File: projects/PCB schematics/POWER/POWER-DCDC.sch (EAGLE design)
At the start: 1 part

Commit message: POWER - DC DC 90% done.
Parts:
- added C1: 1u, rcl:C-USC0805
- added C2, C3: ECA-1VM102B, IowaFormula:ECA-1VM102B
- added F1: 0505030.MXEP, IowaFormula:0505030.MXEP
- added J3, J4: 2P_1-770166-0, con-MATE-N-LOK:2P_1-770166-0
- added R1: PWR221T-30-1R00F, IowaFormula:PWR221T-30-1R00F
- added U$1: DCMHEATSINK, IowaFormula:DCMHEATSINK
- added U$2: SRP1238A-R22M, IowaFormula:SRP1238A-R22M
- added U$3: SRP1238A-4R7M, IowaFormula:SRP1238A-4R7M
- added X1, X2, X3, X4: 5566-2, con-molex:5566-2
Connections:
- new net +12V-ISO: X1-1.S, X1-2.S, X2-1.S, X2-2.S
- new net +12V-OUT: C1.1, C2.1, C3.1, PS1.+OUT_1, R1.1, U$2.1
- new net GND: C1.2, C2.2, C3.2, PS1.-OUT_1, X3-1.S, X3-2.S, X4-1.S, X4-2.S
- new net HV+: F1.1, J3.1, J3.2
- new net HV+_IN: PS1.+IN, U$3.2
- new net HV+_POSTFUSE: F1.2, U$3.1
- new net HV-: J4.1, J4.2, PS1.-IN
- new net N$1: R1.2, U$2.2
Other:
- note added: "30A 0505030.MXEP 500VAC/VDC"
- moved on the sheet: PS1

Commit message: POWER - DCDC Rev A.
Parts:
- removed U$2: SRP1238A-R22M, IowaFormula:SRP1238A-R22M
- removed X3, X4: 5566-2, con-molex:5566-2
- added .GND, >GND: 5566-2, con-molex:5566-2
- added C14, C4, C5, C7: ECA-2WHG2R2, IowaFormula:ECA-2WHG2R2
- added R2: PWR221T-30-1R00F, IowaFormula:PWR221T-30-1R00F
- added U$4: SRP1238A-4R7M, IowaFormula:SRP1238A-4R7M
- C1: value 1u -> ECA-2WHG2R2; device rcl:C-USC0805 -> IowaFormula:ECA-2WHG2R2
- renumbered J3 to HV+, J4 to HV-, X1 to +12V-ISO1, X2 to +12V-ISO2
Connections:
- removed net HV+_IN: PS1.+IN, U$3.2
- net +12V-ISO: now also C14.1, C5.1, R1.2, U$4.2
- net +12V-OUT: now also U$4.1; no longer C1.1, U$2.1
- net GND: now also .GND-1.S, .GND-2.S, >GND-1.S, >GND-2.S, C14.2, C5.2; no longer C1.2, X3-1.S, X3-2.S, X4-1.S, X4-2.S
- net HV+_POSTFUSE: now also R2.2
- net HV-: now also C1.2, C4.2, C7.2
- net N$1: now also C1.1, C4.1, C7.1, PS1.+IN, R2.1, U$3.2; no longer R1.2, U$2.2
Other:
- moved on the sheet: C2, C3, F1, R1, U$3

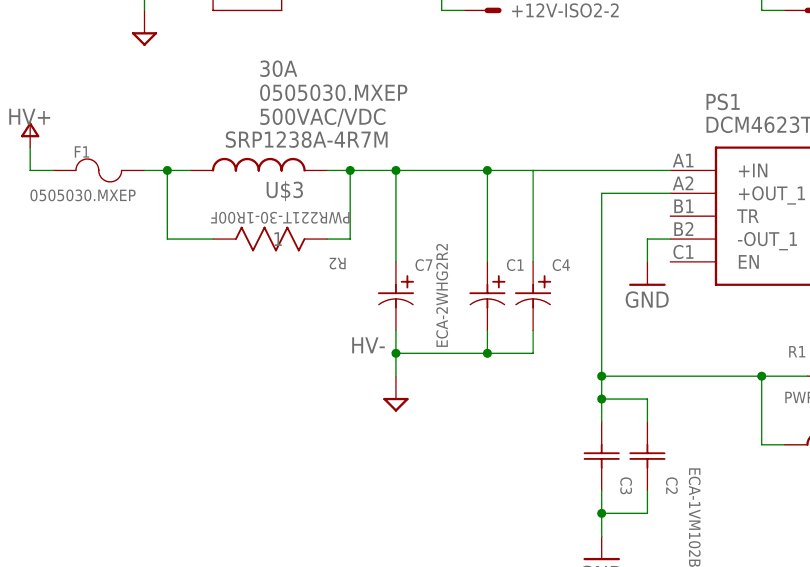
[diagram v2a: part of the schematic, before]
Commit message: POWER - DCDC changes w/ Ryan.
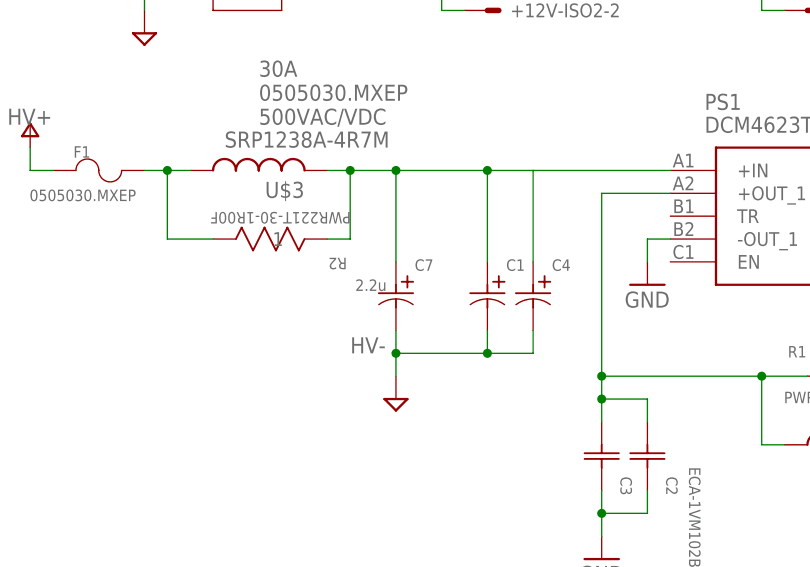
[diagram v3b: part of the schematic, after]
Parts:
- C7: value ECA-2WHG2R2 -> 2.2u
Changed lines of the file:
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@@
 <part name="R1" library="IowaFormula" deviceset="PWR221T-30-1R00F" device=""/>
 <part name="U$3" library="IowaFormula" deviceset="SRP1238A-4R7M" device=""/>
-<part name="C7" library="IowaFormula" deviceset="ECA-2WHG2R2" device=""/>
+<part name="C7" library="IowaFormula" deviceset="ECA-2WHG2R2" device="" value="2.2u"/>
 <part name="SUPPLY3" library="supply2" library_urn="urn:adsk.eagle:library:372" deviceset="AGND" device=""/>
 <part name="R2" library="IowaFormula" deviceset="PWR221T-30-1R00F" device=""/>
@@
 </instance>
 <instance part="C7" gate="A" x="40.64" y="35.56" smashed="yes" rot="R270">
-<attribute name="VALUE" x="46.4058" y="25.9588" size="1.27" layer="96" ratio="10" rot="SR90"/>
+<attribute name="VALUE" x="36.1188" y="32.3342" size="1.27" layer="96" ratio="10" rot="SR0"/>
 <attribute name="NAME" x="42.7228" y="34.5694" size="1.27" layer="96" ratio="10" rot="SR0"/>
 </instance>

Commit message: PROJ - Final pre-purchase revisions (4 boards still in progress.)
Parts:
- renumbered +12V-ISO1 to +12V-ISO.1, +12V-ISO2 to +12V-ISO.2, .GND to GND.2, >GND to GND.1, PS1 to ISO-DCDC, U$1 to HEATSINK
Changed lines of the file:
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@@
 </classes>
 <parts>
-<part name="PS1" library="DCM4623" deviceset="DCM4623TD2K31E0M70" device=""/>
-<part name="+12V-ISO1" library="con-molex" library_urn="urn:adsk.eagle:library:165" deviceset="5566-2" device="" package3d_urn="urn:adsk.eagle:package:8078583/1"/>
-<part name="+12V-ISO2" library="con-molex" library_urn="urn:adsk.eagle:library:165" deviceset="5566-2" device="" package3d_urn="urn:adsk.eagle:package:8078583/1"/>
+<part name="ISO-DCDC" library="DCM4623" deviceset="DCM4623TD2K31E0M70" device=""/>
+<part name="+12V-ISO.1" library="con-molex" library_urn="urn:adsk.eagle:library:165" deviceset="5566-2" device="" package3d_urn="urn:adsk.eagle:package:8078583/1"/>
+<part name="+12V-ISO.2" library="con-molex" library_urn="urn:adsk.eagle:library:165" deviceset="5566-2" device="" package3d_urn="urn:adsk.eagle:package:8078583/1"/>
 <part name="HV+" library="con-MATE-N-LOK" deviceset="2P_1-770166-0" device=""/>
 <part name="HV-" library="con-MATE-N-LOK" deviceset="2P_1-770166-0" device=""/>
-<part name="&gt;GND" library="con-molex" library_urn="urn:adsk.eagle:library:165" deviceset="5566-2" device="" package3d_urn="urn:adsk.eagle:package:8078583/1"/>
-<part name=".GND" library="con-molex" library_urn="urn:adsk.eagle:library:165" deviceset="5566-2" device="" package3d_urn="urn:adsk.eagle:package:8078583/1"/>
+<part name="GND.1" library="con-molex" library_urn="urn:adsk.eagle:library:165" deviceset="5566-2" device="" package3d_urn="urn:adsk.eagle:package:8078583/1"/>
+<part name="GND.2" library="con-molex" library_urn="urn:adsk.eagle:library:165" deviceset="5566-2" device="" package3d_urn="urn:adsk.eagle:package:8078583/1"/>
 <part name="P+1" library="supply1" library_urn="urn:adsk.eagle:library:371" deviceset="V+" device=""/>
 <part name="SUPPLY1" library="supply2" library_urn="urn:adsk.eagle:library:372" deviceset="AGND" device=""/>
 <part name="P+2" library="supply1" library_urn="urn:adsk.eagle:library:371" deviceset="V+" device=""/>
 <part name="F1" library="IowaFormula" deviceset="0505030.MXEP" device=""/>
-<part name="U$1" library="IowaFormula" deviceset="DCMHEATSINK" device=""/>
+<part name="HEATSINK" library="IowaFormula" deviceset="DCMHEATSINK" device=""/>
 <part name="GND2" library="supply1" library_urn="urn:adsk.eagle:library:371" deviceset="GND" device=""/>
 <part name="R1" library="IowaFormula" deviceset="PWR221T-30-1R00F" device=""/>
@@
 </plain>
 <instances>
-<instance part="PS1" gate="G$1" x="71.12" y="45.72" smashed="yes">
+<instance part="ISO-DCDC" gate="G$1" x="71.12" y="45.72" smashed="yes">
 <attribute name="NAME" x="74.93" y="53.34" size="1.778" layer="95" align="center-left"/>
 <attribute name="VALUE" x="74.93" y="50.8" size="1.778" layer="96" align="center-left"/>
 </instance>
-<instance part="+12V-ISO1" gate="-1" x="50.8" y="81.28" smashed="yes">
+<instance part="+12V-ISO.1" gate="-1" x="50.8" y="81.28" smashed="yes">
 <attribute name="NAME" x="53.34" y="80.518" size="1.524" layer="95"/>
 <attribute name="VALUE" x="50.038" y="82.677" size="1.778" layer="96"/>
 </instance>
-<instance part="+12V-ISO1" gate="-2" x="50.8" y="76.2" smashed="yes">
+<instance part="+12V-ISO.1" gate="-2" x="50.8" y="76.2" smashed="yes">
 <attribute name="NAME" x="53.34" y="75.438" size="1.524" layer="95"/>
 <attribute name="VALUE" x="50.038" y="77.597" size="1.778" layer="96"/>
 </instance>
-<instance part="+12V-ISO2" gate="-1" x="50.8" y="68.58" smashed="yes">
+<instance part="+12V-ISO.2" gate="-1" x="50.8" y="68.58" smashed="yes">
 <attribute name="NAME" x="53.34" y="67.818" size="1.524" layer="95"/>
 <attribute name="VALUE" x="50.038" y="69.977" size="1.778" layer="96"/>
 </instance>
-<instance part="+12V-ISO2" gate="-2" x="50.8" y="63.5" smashed="yes">
+<instance part="+12V-ISO.2" gate="-2" x="50.8" y="63.5" smashed="yes">
 <attribute name="NAME" x="53.34" y="62.738" size="1.524" layer="95"/>
 <attribute name="VALUE" x="50.038" y="64.897" size="1.778" layer="96"/>
@@
 <attribute name="NAME" x="19.4056" y="71.3486" size="2.0828" layer="95" ratio="6" rot="SR0"/>
 </instance>
-<instance part="&gt;GND" gate="-1" x="86.36" y="81.28" smashed="yes">
+<instance part="GND.1" gate="-1" x="86.36" y="81.28" smashed="yes">
 <attribute name="NAME" x="88.9" y="80.518" size="1.524" layer="95"/>
 <attribute name="VALUE" x="85.598" y="82.677" size="1.778" layer="96"/>
 </instance>
-<instance part="&gt;GND" gate="-2" x="86.36" y="76.2" smashed="yes">
+<instance part="GND.1" gate="-2" x="86.36" y="76.2" smashed="yes">
 <attribute name="NAME" x="88.9" y="75.438" size="1.524" layer="95"/>
 <attribute name="VALUE" x="85.598" y="77.597" size="1.778" layer="96"/>
 </instance>
-<instance part=".GND" gate="-1" x="86.36" y="68.58" smashed="yes">
+<instance part="GND.2" gate="-1" x="86.36" y="68.58" smashed="yes">
 <attribute name="NAME" x="88.9" y="67.818" size="1.524" layer="95"/>
 <attribute name="VALUE" x="85.598" y="69.977" size="1.778" layer="96"/>
 </instance>
-<instance part=".GND" gate="-2" x="86.36" y="63.5" smashed="yes">
+<instance part="GND.2" gate="-2" x="86.36" y="63.5" smashed="yes">
 <attribute name="NAME" x="88.9" y="62.738" size="1.524" layer="95"/>
 <attribute name="VALUE" x="85.598" y="64.897" size="1.778" layer="96"/>
@@
 <attribute name="NAME" x="4.8006" y="47.1424" size="1.27" layer="95" ratio="10" rot="SR0"/>
 </instance>
-<instance part="U$1" gate="A" x="132.08" y="45.72" smashed="yes"/>
+<instance part="HEATSINK" gate="A" x="132.08" y="45.72" smashed="yes"/>
 <instance part="GND2" gate="1" x="68.58" y="33.02" smashed="yes">
 <attribute name="VALUE" x="66.04" y="30.48" size="1.778" layer="96"/>
@@
 <pinref part="SUPPLY2" gate="G$1" pin="AGND"/>
 <wire x1="111.76" y1="38.1" x2="111.76" y2="35.56" width="0.1524" layer="91"/>
-<pinref part="PS1" gate="G$1" pin="-IN"/>
+<pinref part="ISO-DCDC" gate="G$1" pin="-IN"/>
 <wire x1="104.14" y1="38.1" x2="111.76" y2="38.1" width="0.1524" layer="91"/>
 <label x="111.76" y="38.1" size="1.778" layer="95" rot="MR0"/>
@@
 <wire x1="45.72" y1="76.2" x2="48.26" y2="76.2" width="0.1524" layer="91"/>
 <label x="33.02" y="81.28" size="1.778" layer="95"/>
-<pinref part="+12V-ISO1" gate="-1" pin="S"/>
-<pinref part="+12V-ISO1" gate="-2" pin="S"/>
+<pinref part="+12V-ISO.1" gate="-1" pin="S"/>
+<pinref part="+12V-ISO.1" gate="-2" pin="S"/>
 </segment>
 <segment>
@@
 <wire x1="45.72" y1="63.5" x2="48.26" y2="63.5" width="0.1524" layer="91"/>
 <label x="33.02" y="68.58" size="1.778" layer="95"/>
-<pinref part="+12V-ISO2" gate="-1" pin="S"/>
-<pinref part="+12V-ISO2" gate="-2" pin="S"/>
+<pinref part="+12V-ISO.2" gate="-1" pin="S"/>
+<pinref part="+12V-ISO.2" gate="-2" pin="S"/>
 </segment>
 <segment>
@@
 <wire x1="81.28" y1="76.2" x2="83.82" y2="76.2" width="0.1524" layer="91"/>
 <label x="68.58" y="81.28" size="1.778" layer="95"/>
-<pinref part="&gt;GND" gate="-1" pin="S"/>
-<pinref part="&gt;GND" gate="-2" pin="S"/>
+<pinref part="GND.1" gate="-1" pin="S"/>
+<pinref part="GND.1" gate="-2" pin="S"/>
 </segment>
 <segment>
@@
 <wire x1="81.28" y1="63.5" x2="83.82" y2="63.5" width="0.1524" layer="91"/>
 <label x="68.58" y="68.58" size="1.778" layer="95"/>
-<pinref part=".GND" gate="-1" pin="S"/>
-<pinref part=".GND" gate="-2" pin="S"/>
+<pinref part="GND.2" gate="-1" pin="S"/>
+<pinref part="GND.2" gate="-2" pin="S"/>
 </segment>
 <segment>
 <pinref part="GND2" gate="1" pin="GND"/>
 <wire x1="68.58" y1="35.56" x2="68.58" y2="38.1" width="0.1524" layer="91"/>
-<pinref part="PS1" gate="G$1" pin="-OUT_1"/>
+<pinref part="ISO-DCDC" gate="G$1" pin="-OUT_1"/>
 <wire x1="68.58" y1="38.1" x2="71.12" y2="38.1" width="0.1524" layer="91"/>
 </segment>
@@
 <net name="+12V-OUT" class="0">
 <segment>
-<pinref part="PS1" gate="G$1" pin="+OUT_1"/>
+<pinref part="ISO-DCDC" gate="G$1" pin="+OUT_1"/>
 <wire x1="71.12" y1="43.18" x2="63.5" y2="43.18" width="0.1524" layer="91"/>
 <wire x1="63.5" y1="43.18" x2="63.5" y2="22.86" width="0.1524" layer="91"/>
@@
 <pinref part="C7" gate="A" pin="1"/>
 <wire x1="40.64" y1="45.72" x2="40.64" y2="35.56" width="0.1524" layer="91"/>
-<pinref part="PS1" gate="G$1" pin="+IN"/>
+<pinref part="ISO-DCDC" gate="G$1" pin="+IN"/>
 <wire x1="40.64" y1="45.72" x2="50.8" y2="45.72" width="0.1524" layer="91"/>
 <junction x="40.64" y="45.72"/>

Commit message: PROJ - Gerber files major milestone - 05/05/19.
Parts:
- U$3, U$4: value SRP1238A-4R7M -> SRP1238A-1R0M; device IowaFormula:SRP1238A-4R7M -> IowaFormula:SRP1238A-1R0M
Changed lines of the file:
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@@
 <layer number="97" name="Info" color="7" fill="1" visible="yes" active="yes"/>
 <layer number="98" name="Guide" color="6" fill="1" visible="yes" active="yes"/>
+<layer number="99" name="SpiceOrder" color="5" fill="1" visible="no" active="no"/>
 <layer number="100" name="Muster" color="7" fill="1" visible="no" active="yes"/>
 <layer number="101" name="Patch_Top" color="12" fill="4" visible="no" active="yes"/>
@@
 <part name="GND2" library="supply1" library_urn="urn:adsk.eagle:library:371" deviceset="GND" device=""/>
 <part name="R1" library="IowaFormula" deviceset="PWR221T-30-1R00F" device=""/>
-<part name="U$3" library="IowaFormula" deviceset="SRP1238A-4R7M" device=""/>
+<part name="U$3" library="IowaFormula" deviceset="SRP1238A-1R0M" device=""/>
 <part name="C7" library="IowaFormula" deviceset="ECA-2WHG2R2" device="" value="2.2u"/>
 <part name="SUPPLY3" library="supply2" library_urn="urn:adsk.eagle:library:372" deviceset="AGND" device=""/>
@@
 <part name="C3" library="IowaFormula" deviceset="ECA-1VM102B" device=""/>
 <part name="C14" library="IowaFormula" deviceset="ECA-2WHG2R2" device=""/>
-<part name="U$4" library="IowaFormula" deviceset="SRP1238A-4R7M" device=""/>
+<part name="U$4" library="IowaFormula" deviceset="SRP1238A-1R0M" device=""/>
 <part name="GND3" library="supply1" library_urn="urn:adsk.eagle:library:371" deviceset="GND" device=""/>
 <part name="C1" library="IowaFormula" deviceset="ECA-2WHG2R2" device=""/>
@@
 <pinref part="C4" gate="A" pin="2"/>
 <wire x1="55.88" y1="25.4" x2="55.88" y2="27.94" width="0.1524" layer="91"/>
+<junction x="55.88" y="25.4"/>
 </segment>
 <segment>
@@
 <pinref part="GND1" gate="1" pin="GND"/>
 <wire x1="63.5" y1="7.62" x2="63.5" y2="5.08" width="0.1524" layer="91"/>
+<junction x="68.58" y="7.62"/>
 </segment>
 <segment>
@@
 <wire x1="121.92" y1="7.62" x2="114.3" y2="7.62" width="0.1524" layer="91"/>
 <junction x="114.3" y="7.62"/>
+<junction x="121.92" y="7.62"/>
 </segment>
 </net>
@@
 <pinref part="U$4" gate="G$1" pin="1"/>
 <wire x1="81.28" y1="15.24" x2="83.82" y2="15.24" width="0.1524" layer="91"/>
+<junction x="68.58" y="20.32"/>
 </segment>
 </net>
@@
 <pinref part="C4" gate="A" pin="1"/>
 <wire x1="55.88" y1="45.72" x2="55.88" y2="35.56" width="0.1524" layer="91"/>
+<junction x="55.88" y="45.72"/>
 </segment>
 </net>
@@
 </sheet>
 </sheets>
+<errors>
+</errors>
 </schematic>
 </drawing>
